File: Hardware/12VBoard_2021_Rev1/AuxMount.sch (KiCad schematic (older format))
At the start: 27 parts

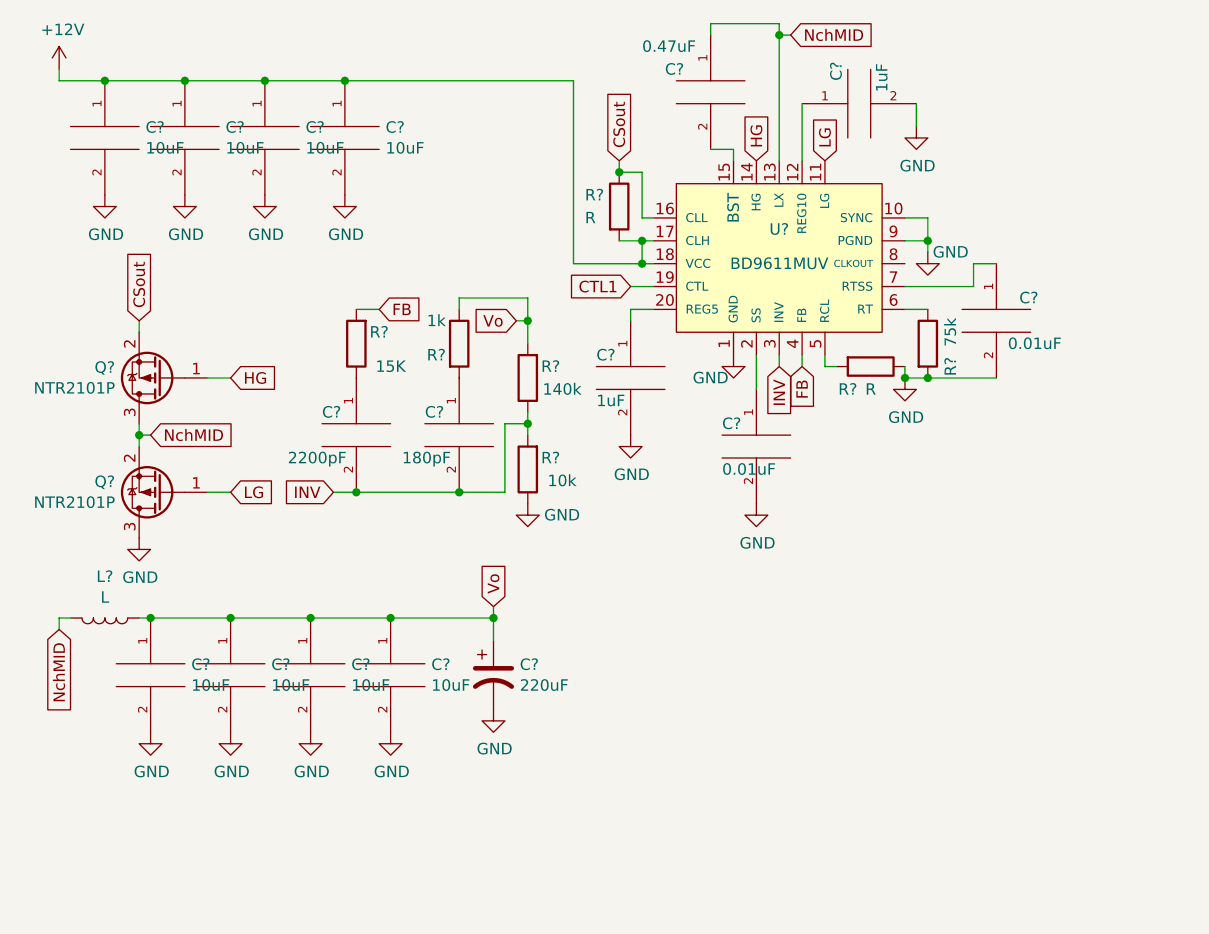
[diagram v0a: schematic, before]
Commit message: current sense
started current sense circuit on hig current. added fuse and LED signal. started tiva wiring.
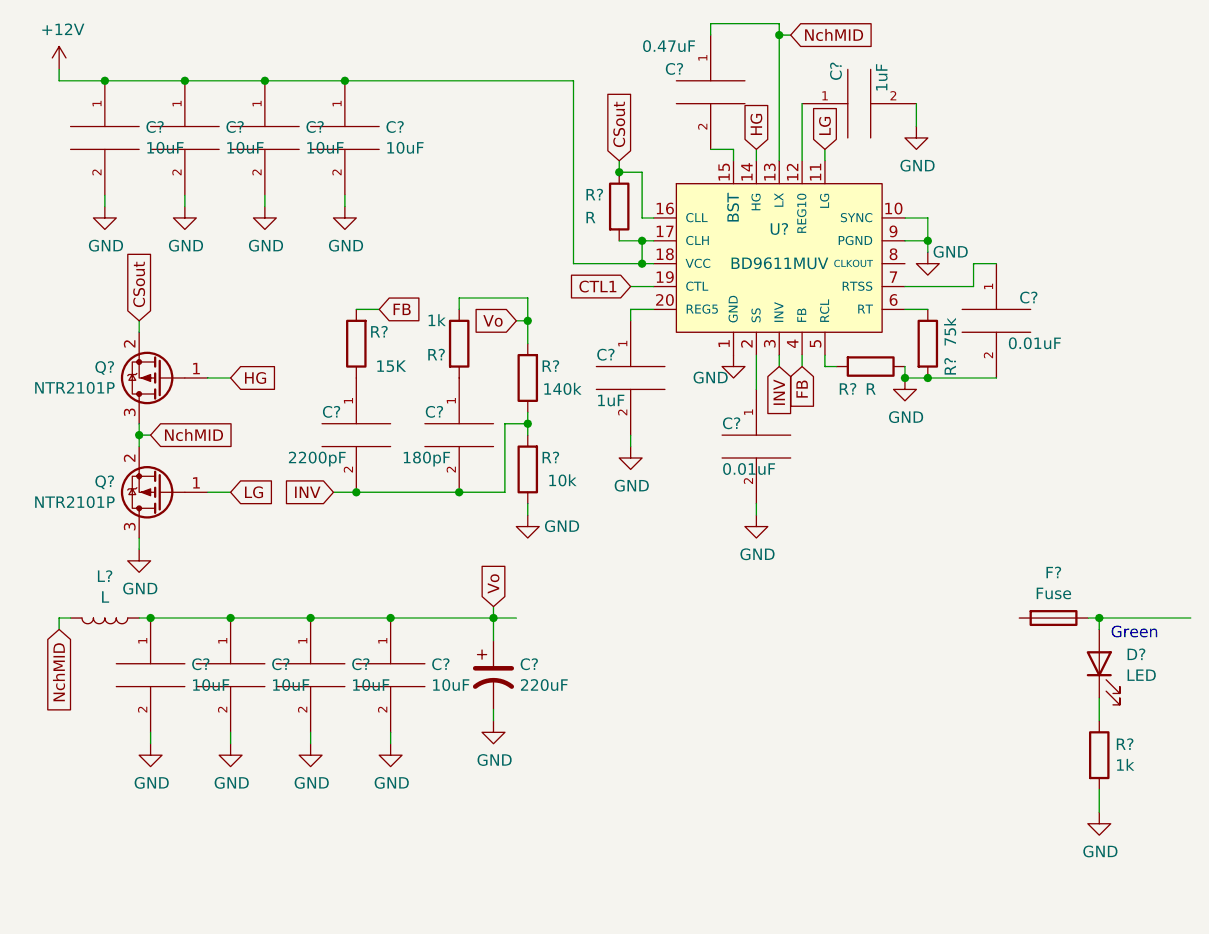
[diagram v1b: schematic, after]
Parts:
- added D?: LED, symbol Device:LED
- added F?: Fuse, symbol Device:Fuse
- added R?: 1k, symbol Device:R
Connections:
- net GND: now also R?.2
- new net: D?.2 (A), F?.1
- new net: D?.1 (K), R?.1
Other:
- note added: "Green"

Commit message: current sense
finished adding current sensing to high current side, also started thinking about tiva pin connector layout
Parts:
- added R?: 5m, symbol Device:R
- added U?: INA198, Package_TO_SOT_SMD:SOT-23-5, symbol Amplifier_Current:INA198
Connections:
- net GND: now also U?.2 (GND)
- net Vo: now also R?.2, U?.4 (+)
- net at F?.2: now also R?.1, U?.5 (-)
- new net 5V: U?.3 (V+)
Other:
- moved on the sheet: D?, F?, R?
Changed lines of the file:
@@
 L Device:Fuse F?
 U 1 1 5F92751C
-P 5100 3200
+P 3900 3200
 AR Path="/5F74F36B/5F821EB2/5F92751C" Ref="F?"  Part="1"
 AR Path="/5F74F36B/5F8222BE/5F92751C" Ref="F?"  Part="1"
-F 0 "F?" V 4903 3200 50  0000 C CNN
-F 1 "Fuse" V 4994 3200 50  0000 C CNN
-F 2 "" V 5030 3200 50  0001 C CNN
-F 3 "~" H 5100 3200 50  0001 C CNN
-	1    5100 3200
+F 0 "F?" V 3703 3200 50  0000 C CNN
+F 1 "Fuse" V 3794 3200 50  0000 C CNN
+F 2 "" V 3830 3200 50  0001 C CNN
+F 3 "~" H 3900 3200 50  0001 C CNN
+	1    3900 3200
 	0    1    1    0
 $EndComp
 Wire Wire Line
-	2750 3200 2650 3200
-Wire Wire Line
-	5250 3200 5300 3200
+	4050 3200 4100 3200
 $Comp
 L Device:R R?
 U 1 1 5F93CBAE
-P 5300 3800
+P 4100 3800
 AR Path="/5F74F36B/5F821EB2/5F93CBAE" Ref="R?"  Part="1"
 AR Path="/5F74F36B/5F8222BE/5F93CBAE" Ref="R?"  Part="1"
-F 0 "R?" H 5370 3846 50  0000 L CNN
-F 1 "1k" H 5370 3755 50  0000 L CNN
-F 2 "" V 5230 3800 50  0001 C CNN
-F 3 "~" H 5300 3800 50  0001 C CNN
-	1    5300 3800
+F 0 "R?" H 4170 3846 50  0000 L CNN
+F 1 "1k" H 4170 3755 50  0000 L CNN
+F 2 "" V 4030 3800 50  0001 C CNN
+F 3 "~" H 4100 3800 50  0001 C CNN
+	1    4100 3800
 	1    0    0    -1
 $EndComp
@@
 L power:GND #PWR?
 U 1 1 5F93CBB4
-P 5300 4050
+P 4100 4050
 AR Path="/5F74F36B/5F821EB2/5F93CBB4" Ref="#PWR?"  Part="1"
 AR Path="/5F74F36B/5F8222BE/5F93CBB4" Ref="#PWR?"  Part="1"
-F 0 "#PWR?" H 5300 3800 50  0001 C CNN
-F 1 "GND" H 5305 3877 50  0000 C CNN
-F 2 "" H 5300 4050 50  0001 C CNN
-F 3 "" H 5300 4050 50  0001 C CNN
-	1    5300 4050
+F 0 "#PWR?" H 4100 3800 50  0001 C CNN
+F 1 "GND" H 4105 3877 50  0000 C CNN
+F 2 "" H 4100 4050 50  0001 C CNN
+F 3 "" H 4100 4050 50  0001 C CNN
+	1    4100 4050
 	1    0    0    -1
 $EndComp
@@
 L Device:LED D?
 U 1 1 5F93CBBA
-P 5300 3400
+P 4100 3400
 AR Path="/5F74F36B/5F821EB2/5F93CBBA" Ref="D?"  Part="1"
 AR Path="/5F74F36B/5F8222BE/5F93CBBA" Ref="D?"  Part="1"
-F 0 "D?" V 5339 3283 50  0000 R CNN
-F 1 "LED" V 5248 3283 50  0000 R CNN
-F 2 "" H 5300 3400 50  0001 C CNN
-F 3 "~" H 5300 3400 50  0001 C CNN
-	1    5300 3400
+F 0 "D?" V 4139 3283 50  0000 R CNN
+F 1 "LED" V 4048 3283 50  0000 R CNN
+F 2 "" H 4100 3400 50  0001 C CNN
+F 3 "~" H 4100 3400 50  0001 C CNN
+	1    4100 3400
 	0    -1   -1   0
 $EndComp
 Wire Wire Line
-	5300 4050 5300 3950
+	4100 4050 4100 3950
 Wire Wire Line
-	5300 3650 5300 3550
+	4100 3650 4100 3550
 Wire Wire Line
-	5300 3250 5300 3200
-Connection ~ 5300 3200
+	4100 3250 4100 3200
+Connection ~ 4100 3200
 Wire Wire Line
-	5300 3200 5700 3200
-Text Notes 5350 3300 0    50   ~ 0
+	4100 3200 4500 3200
+Text Notes 4150 3300 0    50   ~ 0
 Green
+$Comp
+L Amplifier_Current:INA198 U?
+U 1 1 5F8C10CA
+P 3450 3950
+AR Path="/5F74F36B/5F8236F9/5F8C10CA" Ref="U?"  Part="1"
+AR Path="/5F74F36B/5F8222BE/5F8C10CA" Ref="U?"  Part="1"
+F 0 "U?" V 3500 3800 50  0000 R CNN
+F 1 "INA198" V 3600 3900 50  0000 R CNN
+F 2 "Package_TO_SOT_SMD:SOT-23-5" H 3450 3950 50  0001 C CNN
+F 3 "http://www.ti.com/lit/ds/symlink/ina193.pdf" H 3450 3950 50  0001 C CNN
+	1    3450 3950
+	0    -1   1    0
+$EndComp
+$Comp
+L Device:R R?
+U 1 1 5F8C10D0
+P 3450 3200
+AR Path="/5F74F36B/5F8236F9/5F8C10D0" Ref="R?"  Part="1"
+AR Path="/5F74F36B/5F8222BE/5F8C10D0" Ref="R?"  Part="1"
+F 0 "R?" V 3243 3200 50  0000 C CNN
+F 1 "5m" V 3334 3200 50  0000 C CNN
+F 2 "" V 3380 3200 50  0001 C CNN
+F 3 "~" H 3450 3200 50  0001 C CNN
+	1    3450 3200
+	0    1    1    0
+$EndComp
+Wire Wire Line
+	3350 3650 3350 3300
+Wire Wire Line
+	3350 3300 3300 3300
+Wire Wire Line
+	3300 3300 3300 3200
+Connection ~ 3300 3200
+Wire Wire Line
+	3550 3650 3550 3300
+Wire Wire Line
+	3550 3300 3600 3300
+Wire Wire Line
+	3600 3300 3600 3200
+$Comp
+L power:GND #PWR?
+U 1 1 5F8C10DE
+P 3950 3900
+AR Path="/5F74F36B/5F8236F9/5F8C10DE" Ref="#PWR?"  Part="1"
+AR Path="/5F74F36B/5F8222BE/5F8C10DE" Ref="#PWR?"  Part="1"
+F 0 "#PWR?" H 3950 3650 50  0001 C CNN
+F 1 "GND" H 3955 3727 50  0000 C CNN
+F 2 "" H 3950 3900 50  0001 C CNN
+F 3 "" H 3950 3900 50  0001 C CNN
+	1    3950 3900
+	1    0    0    -1
+$EndComp
+Wire Wire Line
+	3950 3900 3950 3850
+Wire Wire Line
+	3950 3850 3750 3850
+Text GLabel 3100 3850 0    50   Input ~ 0
+5V
+Wire Wire Line
+	3150 3850 3100 3850
+Wire Wire Line
+	2650 3200 3300 3200
+Wire Wire Line
+	3750 3200 3600 3200
+Connection ~ 3600 3200
 $EndSCHEMATC

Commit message: High current
Fisnished adding labes/tags
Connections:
- net CTL1 is gone; now on net AuxMountSense: U?.19 (CTL)
- net AuxMountSense: now reaches U?.1
- net 12V15AAuxMount: now reaches D?.2 (A), F?.1
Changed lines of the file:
@@
 $Descr A4 11693 8268
 encoding utf-8
-Sheet 7 8
+Sheet 8 8
 Title ""
 Date ""
@@
 	1    0    0    -1
 $EndComp
-Text GLabel 3250 1750 0    50   Input ~ 0
-CTL1
 $Comp
 L pspice:CAP C?
@@
 Wire Wire Line
 	3950 3850 3750 3850
-Text GLabel 3100 3850 0    50   Input ~ 0
-5V
 Wire Wire Line
 	3150 3850 3100 3850
@@
 	3750 3200 3600 3200
 Connection ~ 3600 3200
+Text HLabel 3100 3850 0    50   Output ~ 0
+5V
+Text HLabel 4500 3200 2    50   Input ~ 0
+12V15AAuxMount
+Text HLabel 3500 4350 2    49   Output ~ 0
+AuxMountSense
+Wire Wire Line
+	3450 4250 3450 4350
+Wire Wire Line
+	3450 4350 3500 4350
+Text HLabel 3250 1750 0    49   Input ~ 0
+AuxMountSense
 $EndSCHEMATC

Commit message: Added Testpoints
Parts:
- added TP? (x2): TestPoint, symbol Connector:TestPoint
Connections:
- net AuxMountSense: now also TP?.1, TP?.1
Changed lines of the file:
@@
 $EndComp
-Wire Wire Line
-	3250 1750 3350 1750
 Wire Wire Line
 	3350 1850 3250 1850
@@
 Wire Wire Line
 	3450 4350 3500 4350
-Text HLabel 3250 1750 0    49   Input ~ 0
+Text HLabel 2900 1750 0    49   Input ~ 0
 AuxMountSense
+$Comp
+L Connector:TestPoint TP?
+U 1 1 5F8E001D
+P 3300 4350
+F 0 "TP?" V 3358 4468 50  0000 L CNN
+F 1 "TestPoint" V 3200 4350 50  0000 L CNN
+F 2 "" H 3500 4350 50  0001 C CNN
+F 3 "~" H 3500 4350 50  0001 C CNN
+	1    3300 4350
+	0    -1   -1   0
+$EndComp
+Wire Wire Line
+	3450 4350 3300 4350
+Connection ~ 3450 4350
+$Comp
+L Connector:TestPoint TP?
+U 1 1 5F8E6C9C
+P 3200 1800
+F 0 "TP?" H 3258 1918 50  0000 L CNN
+F 1 "TestPoint" H 3258 1827 50  0000 L CNN
+F 2 "" H 3400 1800 50  0001 C CNN
+F 3 "~" H 3400 1800 50  0001 C CNN
+	1    3200 1800
+	-1   0    0    1
+$EndComp
+Wire Wire Line
+	2900 1750 3200 1750
+Wire Wire Line
+	3200 1800 3200 1750
+Connection ~ 3200 1750
+Wire Wire Line
+	3200 1750 3350 1750
 $EndSCHEMATC

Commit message: reviewed
review
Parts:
- R?: value 1k -> 1.2k
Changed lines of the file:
@@
 $Descr A4 11693 8268
 encoding utf-8
-Sheet 8 8
+Sheet 7 7
 Title ""
 Date ""
@@
 AR Path="/5F74F36B/5F8222BE/5F93CBAE" Ref="R?"  Part="1"
 F 0 "R?" H 4170 3846 50  0000 L CNN
-F 1 "1k" H 4170 3755 50  0000 L CNN
+F 1 "1.2k" H 4170 3755 50  0000 L CNN
 F 2 "" V 4030 3800 50  0001 C CNN
 F 3 "~" H 4100 3800 50  0001 C CNN
